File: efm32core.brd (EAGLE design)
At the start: 52.1 x 53.3 mm, 66 parts, among them Q1 MMBT5088, U3 USD-SOCKETNEW, X1 48.0MHz, Y1 32.768kHz

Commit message: layout wires
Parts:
- moved C25 0.25 mm to (11.7, 32.8)
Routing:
- net 3.3V-BLE: track 0.00 -> 36.9 mm
- net BLE-USB-: track 0.00 -> 31.6 mm, vias 0 -> 1
- net BLE-USB+: track 0.00 -> 30.6 mm, vias 0 -> 1
- net BLE-RST: track 0.00 -> 25.1 mm, vias 0 -> 2
- net US1_TX: track 15.5 -> 39.7 mm, vias 0 -> 2
- net US1_RX: track 15.5 -> 38.6 mm, vias 0 -> 2
- net BLE-P1_0: track 0.00 -> 7.89 mm
- net 3.3V: track 193.0 -> 195.2 mm
- net I2C0_SCL: track 41.8 -> 41.0 mm

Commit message: layout and refine wires
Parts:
- moved R11 5.59 mm to (18.5, 47.9)
- moved C7 3.70 mm to (20.7, 22.6), turned to 180 degrees
- moved R9 1.65 mm to (22.5, 42.7)
- moved C17 1.20 mm to (21.7, 17.7), turned to 180 degrees
- moved C8 1.09 mm to (42.5, 18.0)
- moved LOGO1 1.02 mm to (22.1, 29.0)
- moved C18 0.81 mm to (18.2, 17.7)
- moved Y1 0.57 mm to (18.5, 15.2)
- moved C12 0.25 mm to (25.1, 11.9)
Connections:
- removed net N$1: JIOH.1
- removed net N$20: R11.1
- removed net PD6: MCU.34
- removed net PD7: MCU.35
- new net IO10: MCU.6, R11.1
- new net IO8: JIOH.1, MCU.4
- new net IO9: JIOH.2, MCU.5
- new net US1_CLK_2: JIOH.6, MCU.49
- new net US1_CS_2: JIOH.3, MCU.50
- new net US1_RX_2: JIOH.5, MCU.34
- new net US1_TX_2: JIOH.4, MCU.35
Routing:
- net US1_RX_2: track 0.00 -> 77.0 mm, vias 0 -> 3
- net US1_TX_2: track 0.00 -> 76.0 mm, vias 0 -> 3
- net IO10: track 0.00 -> 47.4 mm, vias 0 -> 2
- net US1_CLK_2: track 0.00 -> 46.1 mm, vias 0 -> 2
- net IO9: track 0.00 -> 45.4 mm, vias 0 -> 2
- net US1_CS_2: track 0.00 -> 35.6 mm, vias 0 -> 2
- net IO8: track 0.00 -> 34.1 mm, vias 0 -> 2
- net USB_DP: track 56.3 -> 61.7 mm
- net USB_ID: track 46.7 -> 51.8 mm
- net USB_DM: track 62.2 -> 67.0 mm
- net PA2: track 51.6 -> 55.9 mm
- net I2C0_SDA: track 44.9 -> 48.0 mm
- net I2C0_SCL: track 41.0 -> 43.0 mm
- net US1_RX: track 38.6 -> 40.3 mm
- net US1_TX: track 39.7 -> 41.2 mm
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
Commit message: some refines
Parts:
- moved C20 2.29 mm to (45.7, 38.4)
- moved R7 1.63 mm to (41.1, 46.0)
- moved R8 1.44 mm to (41.1, 43.9)
- moved C22 1.27 mm to (44.2, 40.9)
- moved MPU9150 1.25 mm to (41.0, 38.6)
- moved C21 1.20 mm to (42.5, 35.2)
- moved C19 1.14 mm to (37.3, 37.6)
- moved R4 0.72 mm to (44.5, 43.9)
- moved R5 0.57 mm to (44.5, 46.0)
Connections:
- removed net US1_CLK_2: JIOH.6, MCU.49
- removed net US1_CS_2: JIOH.3, MCU.50
- removed net US1_RX_2: JIOH.5, MCU.34
- removed net US1_TX_2: JIOH.4, MCU.35
- new net US0_CLK: JIOH.6, MCU.61
- new net US0_CS: JIOH.3, MCU.62
- net US0_RX: now also JIOH.5
- net US0_TX: now also JIOH.4
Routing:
- net US1_RX_2: track 77.0 -> 0.00 mm, vias 3 -> 0
- net US1_TX_2: track 76.0 -> 0.00 mm, vias 3 -> 0
- net US0_CLK: track 0.00 -> 49.6 mm, vias 0 -> 2
- net US1_CLK_2: track 46.1 -> 0.00 mm, vias 2 -> 0
- net US0_CS: track 0.00 -> 44.6 mm, vias 0 -> 3
- net US0_RX: track 0.00 -> 36.4 mm, vias 0 -> 2
- net US0_TX: track 0.00 -> 35.7 mm, vias 0 -> 2
- net US1_CS_2: track 35.6 -> 0.00 mm, vias 2 -> 0
- net 3.3V: track 195.8 -> 210.3 mm
- net USB_ID: track 51.8 -> 54.7 mm
- net I2C0_SCL: track 43.0 -> 45.2 mm
- net BLE-USB+: track 30.2 -> 32.0 mm
- net PA2: track 55.9 -> 54.5 mm
- net USB_DP: track 61.7 -> 63.1 mm
- net N$9: track 5.70 -> 5.06 mm
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
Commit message: layout wires, needs refine
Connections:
- removed net N$3: JIOL.1
- new net LEU0_RX_2: JIOL.1, MCU.64
- new net LEU0_TX_2: JIOL.2, MCU.63
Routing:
- net LEU0_RX_2: track 0.00 -> 40.8 mm, vias 0 -> 3
- net LEU0_TX_2: track 0.00 -> 37.4 mm, vias 0 -> 2
- net GND: track 27.3 -> 32.4 mm
- net 3.3V: track 210.3 -> 211.9 mm
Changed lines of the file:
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@@
 </elements>
 <signals>
-<signal name="N$3">
-<contactref element="JIOL" pad="1"/>
-</signal>
 <signal name="3.3V">
 <contactref element="PMIC1" pad="2"/>
@@
 <wire x1="40.271" y1="36.608" x2="40.271" y2="34.937" width="0.3048" layer="1"/>
 <wire x1="35.56" y1="35.941" x2="35.56" y2="39.37" width="0.3048" layer="1"/>
-<wire x1="43.021" y1="37.358" x2="43.922" y2="37.866" width="0.3048" layer="1"/>
-<wire x1="43.922" y1="37.866" x2="44.704" y2="37.084" width="0.3048" layer="1"/>
-<wire x1="44.704" y1="37.084" x2="44.704" y2="34.798" width="0.3048" layer="1"/>
+<wire x1="43.021" y1="37.358" x2="43.561" y2="37.358" width="0.3048" layer="1"/>
+<wire x1="43.561" y1="37.358" x2="44.049" y2="37.358" width="0.3048" layer="1"/>
+<wire x1="44.049" y1="37.358" x2="44.704" y2="36.703" width="0.3048" layer="1"/>
+<wire x1="44.704" y1="36.703" x2="44.704" y2="34.798" width="0.3048" layer="1"/>
 <wire x1="44.704" y1="34.798" x2="44.069" y2="34.163" width="0.3048" layer="1"/>
 <wire x1="44.069" y1="34.163" x2="41.045" y2="34.163" width="0.3048" layer="1"/>
@@
 <wire x1="37.465" y1="42.291" x2="35.56" y2="40.386" width="0.2032" layer="1"/>
 <wire x1="35.56" y1="40.386" x2="35.56" y2="39.37" width="0.2032" layer="1"/>
-<wire x1="44.704" y1="37.084" x2="45.72" y2="37.504" width="0" layer="19" extent="1-1"/>
+<wire x1="45.72" y1="37.504" x2="45.574" y2="37.358" width="0.2032" layer="1"/>
+<wire x1="45.574" y1="37.358" x2="43.561" y2="37.358" width="0.3048" layer="1"/>
 </signal>
 <signal name="VDD">
@@
 <via x="48.514" y="39.37" extent="1-16" drill="0.5"/>
 <via x="37.465" y="40.767" extent="1-16" drill="0.5"/>
-<via x="28.956" y="38.227" extent="1-16" drill="0.5"/>
+<via x="21.082" y="35.179" extent="1-16" drill="0.5"/>
 <via x="31.242" y="13.716" extent="1-16" drill="0.5"/>
 <wire x1="31.77" y1="15.586" x2="31.77" y2="14.244" width="0.254" layer="1"/>
@@
 <via x="32.004" y="31.369" extent="1-16" drill="0.5"/>
 <via x="43.688" y="42.926" extent="1-16" drill="0.5"/>
+<wire x1="43.021" y1="39.358" x2="43.021" y2="39.858" width="0.2032" layer="1"/>
+<wire x1="43.021" y1="39.358" x2="44.069" y2="39.358" width="0.2032" layer="1"/>
+<wire x1="44.069" y1="39.358" x2="45.566" y2="39.358" width="0.2032" layer="1"/>
+<wire x1="45.566" y1="39.358" x2="45.72" y2="39.204" width="0.2032" layer="1"/>
 <wire x1="43.688" y1="42.926" x2="43.6" y2="43.942" width="0" layer="19" extent="1-1"/>
 <wire x1="45.046" y1="40.894" x2="43.688" y2="42.926" width="0" layer="19" extent="1-1"/>
-<wire x1="45.72" y1="39.204" x2="45.046" y2="40.894" width="0" layer="19" extent="1-1"/>
-<wire x1="43.021" y1="39.858" x2="45.046" y2="40.894" width="0" layer="19" extent="1-1"/>
-<wire x1="43.021" y1="39.358" x2="43.021" y2="39.858" width="0" layer="19" extent="1-1"/>
-<wire x1="43.021" y1="38.358" x2="43.021" y2="39.358" width="0" layer="19" extent="1-1"/>
+<wire x1="45.566" y1="39.358" x2="45.046" y2="40.894" width="0" layer="19" extent="1-1"/>
 <wire x1="48.514" y1="39.37" x2="45.72" y2="39.204" width="0" layer="19" extent="1-1"/>
 <wire x1="43.395" y1="35.179" x2="43.021" y2="38.358" width="0" layer="19" extent="1-1"/>
@@
 <wire x1="21.971" y1="39.497" x2="17.78" y2="35.306" width="0" layer="19" extent="1-1"/>
 <wire x1="23.368" y1="40.386" x2="21.971" y2="39.497" width="0" layer="19" extent="1-1"/>
-<wire x1="28.956" y1="38.227" x2="23.368" y2="40.386" width="0" layer="19" extent="1-1"/>
+<wire x1="21.082" y1="35.179" x2="23.368" y2="40.386" width="0" layer="19" extent="1-1"/>
 <wire x1="20.828" y1="46.316" x2="23.368" y2="40.386" width="0" layer="19" extent="1-1"/>
 <wire x1="18.194" y1="45.752" x2="20.828" y2="46.316" width="0" layer="19" extent="1-1"/>
@@
 <wire x1="43.522" y1="27.432" x2="43.522" y2="25.4" width="0" layer="19" extent="1-1"/>
 <wire x1="42.545" y1="16.634" x2="43.522" y2="22.098" width="0" layer="19" extent="1-1"/>
+<wire x1="43.021" y1="38.358" x2="43.819" y2="38.358" width="0.2032" layer="1"/>
+<wire x1="43.819" y1="38.358" x2="44.069" y2="38.608" width="0.2032" layer="1"/>
+<wire x1="44.069" y1="38.608" x2="44.069" y2="39.358" width="0.2032" layer="1"/>
 </signal>
 <signal name="5V">
@@
 <wire x1="31.75" y1="33.401" x2="32.004" y2="33.401" width="0.2032" layer="16"/>
 </signal>
+<signal name="LEU0_RX_2">
+<contactref element="MCU" pad="64"/>
+<contactref element="JIOL" pad="1"/>
+<wire x1="29.27" y1="27.086" x2="27.397" y2="27.086" width="0.2032" layer="1"/>
+<wire x1="27.397" y1="27.086" x2="26.416" y2="28.067" width="0.2032" layer="1"/>
+<wire x1="26.416" y1="28.067" x2="26.416" y2="30.353" width="0.2032" layer="1"/>
+<wire x1="26.416" y1="30.353" x2="27.051" y2="30.988" width="0.2032" layer="1"/>
+<wire x1="27.051" y1="30.988" x2="27.051" y2="32.258" width="0.2032" layer="1"/>
+<wire x1="27.051" y1="32.258" x2="28.448" y2="33.655" width="0.2032" layer="1"/>
+<wire x1="28.448" y1="33.655" x2="28.448" y2="37.973" width="0.2032" layer="1"/>
+<wire x1="28.448" y1="37.973" x2="28.829" y2="38.354" width="0.2032" layer="1"/>
+<via x="28.829" y="38.354" extent="1-16" drill="0.381"/>
+<wire x1="28.829" y1="38.354" x2="33.147" y2="38.354" width="0.2032" layer="16"/>
+<via x="33.147" y="38.354" extent="1-16" drill="0.381"/>
+<wire x1="33.147" y1="38.354" x2="33.147" y2="42.037" width="0.2032" layer="1"/>
+<wire x1="33.147" y1="42.037" x2="35.052" y2="43.942" width="0.2032" layer="1"/>
+<wire x1="35.052" y1="43.942" x2="35.052" y2="45.212" width="0.2032" layer="1"/>
+<wire x1="35.052" y1="45.212" x2="37.211" y2="47.371" width="0.2032" layer="1"/>
+<via x="37.211" y="47.371" extent="1-16" drill="0.381"/>
+<wire x1="37.211" y1="47.371" x2="43.561" y2="47.371" width="0.2032" layer="16"/>
+<wire x1="43.561" y1="47.371" x2="46.99" y2="50.8" width="0.2032" layer="16"/>
+</signal>
+<signal name="LEU0_TX_2">
+<contactref element="MCU" pad="63"/>
+<contactref element="JIOL" pad="2"/>
+<wire x1="29.77" y1="27.086" x2="29.77" y2="28.142" width="0.2032" layer="1"/>
+<wire x1="29.77" y1="28.142" x2="29.591" y2="28.321" width="0.2032" layer="1"/>
+<wire x1="29.591" y1="28.321" x2="27.559" y2="28.321" width="0.2032" layer="1"/>
+<wire x1="27.559" y1="28.321" x2="26.924" y2="28.956" width="0.2032" layer="1"/>
+<wire x1="26.924" y1="28.956" x2="26.924" y2="30.099" width="0.2032" layer="1"/>
+<wire x1="26.924" y1="30.099" x2="27.559" y2="30.734" width="0.2032" layer="1"/>
+<wire x1="27.559" y1="30.734" x2="27.559" y2="32.004" width="0.2032" layer="1"/>
+<wire x1="27.559" y1="32.004" x2="28.956" y2="33.401" width="0.2032" layer="1"/>
+<wire x1="28.956" y1="33.401" x2="28.956" y2="36.703" width="0.2032" layer="1"/>
+<wire x1="28.956" y1="36.703" x2="29.591" y2="37.338" width="0.2032" layer="1"/>
+<via x="29.591" y="37.338" extent="1-16" drill="0.381"/>
+<wire x1="29.591" y1="37.338" x2="34.544" y2="37.338" width="0.2032" layer="16"/>
+<via x="34.544" y="37.338" extent="1-16" drill="0.381"/>
+<wire x1="34.544" y1="37.338" x2="34.544" y2="42.672" width="0.2032" layer="1"/>
+<wire x1="34.544" y1="42.672" x2="40.767" y2="48.895" width="0.2032" layer="1"/>
+<wire x1="40.767" y1="48.895" x2="42.672" y2="48.895" width="0.2032" layer="1"/>
+<wire x1="42.672" y1="48.895" x2="44.45" y2="50.673" width="0.2032" layer="1"/>
+<wire x1="44.45" y1="50.673" x2="44.45" y2="50.8" width="0.2032" layer="1"/>
+</signal>
 </signals>

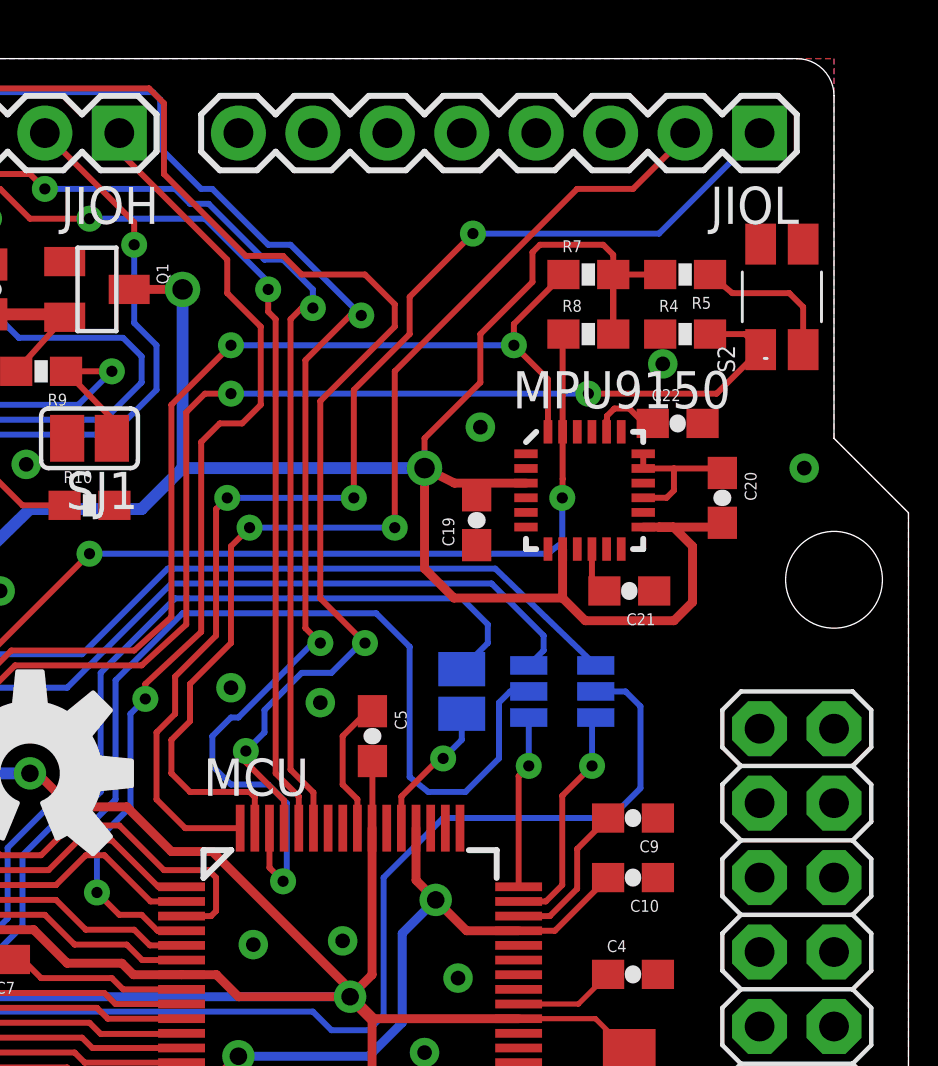
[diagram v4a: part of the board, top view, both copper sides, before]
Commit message: update swd wires
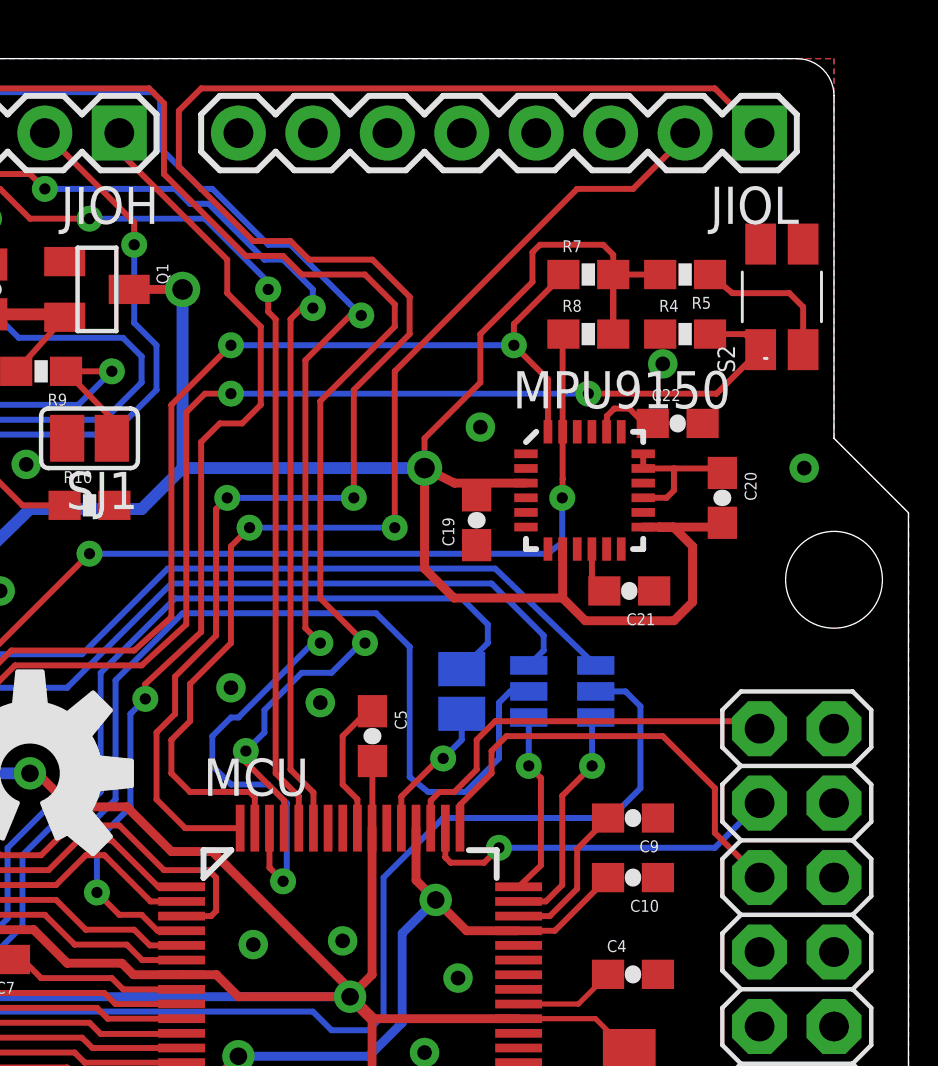
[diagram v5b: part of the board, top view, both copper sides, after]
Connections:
- new net N$10: MCU.54
- new net N$11: MCU.57
- new net N$16: MCU.58
- new net N$17: JEX.11
- new net N$18: JEX.13
- new net N$20: JEX.15
- new net SWCLK: JEX.12, MCU.49
- new net SWIO: JEX.14, MCU.50
- new net SWO: JEX.16, MCU.51
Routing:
- net LEU0_RX_2: track 40.8 -> 58.9 mm, vias 3 -> 2
- net SWCLK: track 0.00 -> 15.3 mm
- net SWO: track 0.00 -> 14.0 mm
- net SWIO: track 0.00 -> 12.6 mm, vias 0 -> 1
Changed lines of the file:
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@@
 <wire x1="44.069" y1="39.358" x2="45.566" y2="39.358" width="0.2032" layer="1"/>
 <wire x1="45.566" y1="39.358" x2="45.72" y2="39.204" width="0.2032" layer="1"/>
+<wire x1="43.021" y1="38.358" x2="43.819" y2="38.358" width="0.2032" layer="1"/>
+<wire x1="43.819" y1="38.358" x2="44.069" y2="38.608" width="0.2032" layer="1"/>
+<wire x1="44.069" y1="38.608" x2="44.069" y2="39.358" width="0.2032" layer="1"/>
 <wire x1="43.688" y1="42.926" x2="43.6" y2="43.942" width="0" layer="19" extent="1-1"/>
 <wire x1="45.046" y1="40.894" x2="43.688" y2="42.926" width="0" layer="19" extent="1-1"/>
 <wire x1="45.566" y1="39.358" x2="45.046" y2="40.894" width="0" layer="19" extent="1-1"/>
 <wire x1="48.514" y1="39.37" x2="45.72" y2="39.204" width="0" layer="19" extent="1-1"/>
-<wire x1="43.395" y1="35.179" x2="43.021" y2="38.358" width="0" layer="19" extent="1-1"/>
+<wire x1="43.395" y1="35.179" x2="43.819" y2="38.358" width="0" layer="19" extent="1-1"/>
 <wire x1="37.465" y1="40.767" x2="43.021" y2="39.858" width="0" layer="19" extent="1-1"/>
 <wire x1="37.338" y1="36.742" x2="37.465" y2="40.767" width="0" layer="19" extent="1-1"/>
@@
 <wire x1="14.732" y1="38.862" x2="12.244" y2="35.352" width="0" layer="19" extent="1-1"/>
 <wire x1="17.78" y1="35.306" x2="14.732" y2="38.862" width="0" layer="19" extent="1-1"/>
-<wire x1="21.971" y1="39.497" x2="17.78" y2="35.306" width="0" layer="19" extent="1-1"/>
+<wire x1="21.082" y1="35.179" x2="17.78" y2="35.306" width="0" layer="19" extent="1-1"/>
+<wire x1="21.971" y1="39.497" x2="21.082" y2="35.179" width="0" layer="19" extent="1-1"/>
 <wire x1="23.368" y1="40.386" x2="21.971" y2="39.497" width="0" layer="19" extent="1-1"/>
-<wire x1="21.082" y1="35.179" x2="23.368" y2="40.386" width="0" layer="19" extent="1-1"/>
 <wire x1="20.828" y1="46.316" x2="23.368" y2="40.386" width="0" layer="19" extent="1-1"/>
 <wire x1="18.194" y1="45.752" x2="20.828" y2="46.316" width="0" layer="19" extent="1-1"/>
@@
 <wire x1="43.522" y1="27.432" x2="43.522" y2="25.4" width="0" layer="19" extent="1-1"/>
 <wire x1="42.545" y1="16.634" x2="43.522" y2="22.098" width="0" layer="19" extent="1-1"/>
-<wire x1="43.021" y1="38.358" x2="43.819" y2="38.358" width="0.2032" layer="1"/>
-<wire x1="43.819" y1="38.358" x2="44.069" y2="38.608" width="0.2032" layer="1"/>
-<wire x1="44.069" y1="38.608" x2="44.069" y2="39.358" width="0.2032" layer="1"/>
 </signal>
 <signal name="5V">
@@
 <contactref element="MCU" pad="48"/>
 <contactref element="JP2" pad="3"/>
-<wire x1="38.77" y1="25.086" x2="38.77" y2="28.864" width="0.2032" layer="1"/>
-<wire x1="38.77" y1="28.864" x2="39.116" y2="29.21" width="0.2032" layer="1"/>
+<wire x1="38.77" y1="25.086" x2="39.532" y2="25.816" width="0.2032" layer="1"/>
 <via x="39.116" y="29.21" extent="1-16" drill="0.381"/>
 <wire x1="39.116" y1="29.21" x2="39.116" y2="30.861" width="0.2032" layer="16"/>
+<wire x1="39.532" y1="25.816" x2="39.532" y2="28.794" width="0.2032" layer="1"/>
+<wire x1="39.532" y1="28.794" x2="39.116" y2="29.21" width="0.2032" layer="1"/>
 </signal>
 <signal name="M_USB_DM">
@@
 <wire x1="33.147" y1="42.037" x2="35.052" y2="43.942" width="0.2032" layer="1"/>
 <wire x1="35.052" y1="43.942" x2="35.052" y2="45.212" width="0.2032" layer="1"/>
-<wire x1="35.052" y1="45.212" x2="37.211" y2="47.371" width="0.2032" layer="1"/>
-<via x="37.211" y="47.371" extent="1-16" drill="0.381"/>
-<wire x1="37.211" y1="47.371" x2="43.561" y2="47.371" width="0.2032" layer="16"/>
-<wire x1="43.561" y1="47.371" x2="46.99" y2="50.8" width="0.2032" layer="16"/>
+<wire x1="35.052" y1="45.212" x2="33.782" y2="46.482" width="0.2032" layer="1"/>
+<wire x1="33.782" y1="46.482" x2="31.623" y2="46.482" width="0.2032" layer="1"/>
+<wire x1="31.623" y1="46.482" x2="30.988" y2="47.117" width="0.2032" layer="1"/>
+<wire x1="30.988" y1="47.117" x2="29.718" y2="47.117" width="0.2032" layer="1"/>
+<wire x1="29.718" y1="47.117" x2="27.178" y2="49.657" width="0.2032" layer="1"/>
+<wire x1="27.178" y1="49.657" x2="27.178" y2="51.562" width="0.2032" layer="1"/>
+<wire x1="27.178" y1="51.562" x2="27.94" y2="52.324" width="0.2032" layer="1"/>
+<wire x1="27.94" y1="52.324" x2="45.466" y2="52.324" width="0.2032" layer="1"/>
+<wire x1="45.466" y1="52.324" x2="46.99" y2="50.8" width="0.2032" layer="1"/>
 </signal>
 <signal name="LEU0_TX_2">
@@
 <wire x1="44.45" y1="50.673" x2="44.45" y2="50.8" width="0.2032" layer="1"/>
 </signal>
+<signal name="N$10">
+<contactref element="MCU" pad="54"/>
+</signal>
+<signal name="N$11">
+<contactref element="MCU" pad="57"/>
+</signal>
+<signal name="N$16">
+<contactref element="MCU" pad="58"/>
+</signal>
+<signal name="N$17">
+<contactref element="JEX" pad="11"/>
+</signal>
+<signal name="N$18">
+<contactref element="JEX" pad="13"/>
+</signal>
+<signal name="N$20">
+<contactref element="JEX" pad="15"/>
+</signal>
+<signal name="SWIO">
+<contactref element="JEX" pad="14"/>
+<contactref element="MCU" pad="50"/>
+<wire x1="36.27" y1="27.086" x2="36.27" y2="26.087" width="0.2032" layer="1"/>
+<wire x1="36.27" y1="26.087" x2="36.449" y2="25.908" width="0.2032" layer="1"/>
+<wire x1="36.449" y1="25.908" x2="37.592" y2="25.908" width="0.2032" layer="1"/>
+<wire x1="37.592" y1="25.908" x2="38.1" y2="26.416" width="0.2032" layer="1"/>
+<via x="38.1" y="26.416" extent="1-16" drill="0.381"/>
+<wire x1="38.1" y1="26.416" x2="45.466" y2="26.416" width="0.2032" layer="16"/>
+<wire x1="45.466" y1="26.416" x2="46.99" y2="27.94" width="0.2032" layer="16"/>
+</signal>
+<signal name="SWO">
+<contactref element="JEX" pad="16"/>
+<contactref element="MCU" pad="51"/>
+<wire x1="35.77" y1="27.086" x2="35.77" y2="28.023" width="0.2032" layer="1"/>
+<wire x1="35.77" y1="28.023" x2="36.068" y2="28.321" width="0.2032" layer="1"/>
+<wire x1="36.068" y1="28.321" x2="36.576" y2="28.321" width="0.2032" layer="1"/>
+<wire x1="36.576" y1="28.321" x2="37.338" y2="29.083" width="0.2032" layer="1"/>
+<wire x1="37.338" y1="29.083" x2="37.338" y2="30.099" width="0.2032" layer="1"/>
+<wire x1="37.338" y1="30.099" x2="37.973" y2="30.734" width="0.2032" layer="1"/>
+<wire x1="37.973" y1="30.734" x2="46.736" y2="30.734" width="0.2032" layer="1"/>
+<wire x1="46.736" y1="30.734" x2="46.99" y2="30.48" width="0.2032" layer="1"/>
+</signal>
+<signal name="SWCLK">
+<contactref element="JEX" pad="12"/>
+<contactref element="MCU" pad="49"/>
+<wire x1="36.77" y1="27.086" x2="36.77" y2="27.88" width="0.2032" layer="1"/>
+<wire x1="36.77" y1="27.88" x2="37.846" y2="28.956" width="0.2032" layer="1"/>
+<wire x1="37.846" y1="28.956" x2="37.846" y2="29.718" width="0.2032" layer="1"/>
+<wire x1="37.846" y1="29.718" x2="38.354" y2="30.226" width="0.2032" layer="1"/>
+<wire x1="38.354" y1="30.226" x2="43.688" y2="30.226" width="0.2032" layer="1"/>
+<wire x1="43.688" y1="30.226" x2="45.466" y2="28.448" width="0.2032" layer="1"/>
+<wire x1="45.466" y1="28.448" x2="45.466" y2="26.924" width="0.2032" layer="1"/>
+<wire x1="45.466" y1="26.924" x2="46.99" y2="25.4" width="0.2032" layer="1"/>
+</signal>
 </signals>
